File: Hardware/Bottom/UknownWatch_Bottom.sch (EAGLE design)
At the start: 31 parts, among them U1 AD5242-SO16

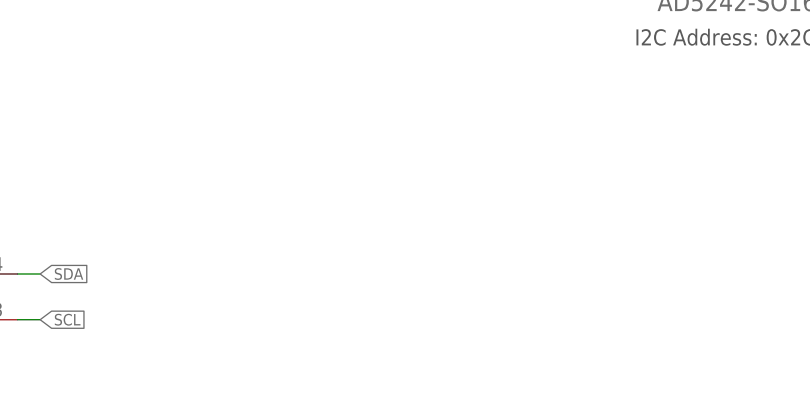
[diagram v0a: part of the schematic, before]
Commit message: Added connections from bottom to top board and other various changes.
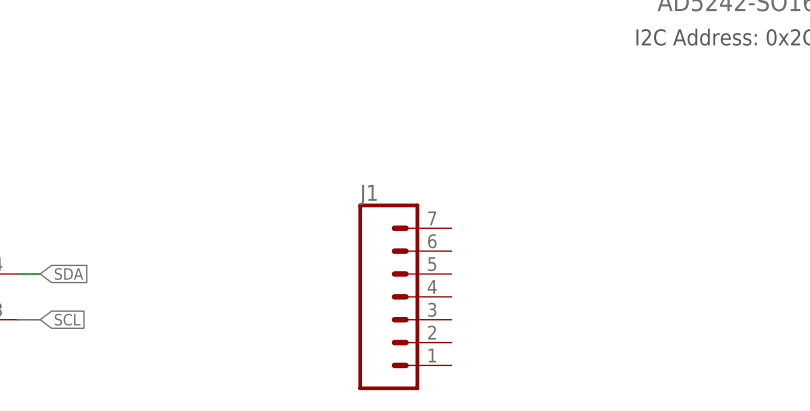
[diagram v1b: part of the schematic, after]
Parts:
- added J1: (no value), LinnesLab-Connectors:CONN_07
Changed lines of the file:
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@@
 <part name="GND2" library="LinnesLab-Symbols" deviceset="GND" device=""/>
 <part name="SUPPLY3" library="LinnesLab-Symbols" deviceset="3.3V" device=""/>
+<part name="J1" library="LinnesLab-Connectors" deviceset="CONN_07" device=""/>
 </parts>
 <sheets>
@@
 <attribute name="VALUE" x="5.08" y="-12.446" size="1.778" layer="96" align="bottom-center"/>
 </instance>
+<instance part="J1" gate="G$1" x="86.36" y="-25.4" smashed="yes">
+<attribute name="VALUE" x="81.28" y="-35.306" size="1.778" layer="96" font="vector"/>
+<attribute name="NAME" x="81.28" y="-12.192" size="1.778" layer="95" font="vector"/>
+</instance>
 </instances>

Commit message: Made all changes associated wih take 002
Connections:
- removed net LED.CTRL: U$4.A
- removed net TIA: C10.2, C15.1, OP4G$1.OUT, U1.W1
- new net A6/TIA: C10.2, C15.1, J1.5, OP4G$1.OUT, U1.W1
- new net A7/PPG: C21.2, J1.7, OP3G$1.OUT
- new net D29/LED.CTRL: J1.6, U$4.A
- net PPG: no longer C21.2, OP3G$1.OUT
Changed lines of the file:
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@@
 </segment>
 </net>
-<net name="TIA" class="0">
+<net name="A6/TIA" class="0">
 <segment>
 <wire x1="109.22" y1="27.94" x2="104.14" y2="27.94" width="0.1524" layer="91"/>
@@
 <junction x="55.88" y="93.98"/>
 </segment>
+<segment>
+<pinref part="J1" gate="G$1" pin="5"/>
+<wire x1="91.44" y1="-20.32" x2="93.98" y2="-20.32" width="0.1524" layer="91"/>
+<label x="93.98" y="-20.32" size="1.27" layer="95" xref="yes"/>
+</segment>
 </net>
 <net name="PD.C" class="0">
@@
 </segment>
 </net>
-<net name="LED.CTRL" class="0">
+<net name="D29/LED.CTRL" class="0">
 <segment>
 <pinref part="U$4" gate="G$1" pin="A"/>
@@
 <wire x1="205.74" y1="30.48" x2="205.74" y2="38.1" width="0.1524" layer="91"/>
 <label x="205.74" y="38.1" size="1.27" layer="95" rot="R180" xref="yes"/>
+</segment>
+<segment>
+<pinref part="J1" gate="G$1" pin="6"/>
+<wire x1="91.44" y1="-17.78" x2="93.98" y2="-17.78" width="0.1524" layer="91"/>
+<label x="93.98" y="-17.78" size="1.27" layer="95" xref="yes"/>
 </segment>
 </net>
@@
 <label x="139.7" y="27.94" size="1.27" layer="95" xref="yes"/>
 <pinref part="U1" gate="G$1" pin="B2"/>
-</segment>
-<segment>
-<pinref part="C21" gate="G$1" pin="2"/>
-<wire x1="187.96" y1="96.52" x2="195.58" y2="96.52" width="0.1524" layer="91"/>
-<wire x1="195.58" y1="96.52" x2="195.58" y2="86.36" width="0.1524" layer="91"/>
-<pinref part="OP3" gate="G$1" pin="OUT"/>
-<wire x1="195.58" y1="86.36" x2="193.04" y2="86.36" width="0.1524" layer="91"/>
-<wire x1="195.58" y1="96.52" x2="195.58" y2="106.68" width="0.1524" layer="91"/>
-<junction x="195.58" y="96.52"/>
-<label x="195.58" y="106.68" size="1.27" layer="95" rot="R180" xref="yes"/>
-<label x="195.58" y="86.36" size="1.27" layer="95" xref="yes"/>
 </segment>
 </net>
@@
 </segment>
 </net>
+<net name="A7/PPG" class="0">
+<segment>
+<pinref part="C21" gate="G$1" pin="2"/>
+<wire x1="187.96" y1="96.52" x2="195.58" y2="96.52" width="0.1524" layer="91"/>
+<wire x1="195.58" y1="96.52" x2="195.58" y2="86.36" width="0.1524" layer="91"/>
+<pinref part="OP3" gate="G$1" pin="OUT"/>
+<wire x1="195.58" y1="86.36" x2="193.04" y2="86.36" width="0.1524" layer="91"/>
+<wire x1="195.58" y1="96.52" x2="195.58" y2="106.68" width="0.1524" layer="91"/>
+<junction x="195.58" y="96.52"/>
+<label x="195.58" y="106.68" size="1.27" layer="95" rot="R180" xref="yes"/>
+<label x="195.58" y="86.36" size="1.27" layer="95" xref="yes"/>
+</segment>
+<segment>
+<pinref part="J1" gate="G$1" pin="7"/>
+<wire x1="91.44" y1="-15.24" x2="93.98" y2="-15.24" width="0.1524" layer="91"/>
+<label x="93.98" y="-15.24" size="1.27" layer="95" xref="yes"/>
+</segment>
+</net>

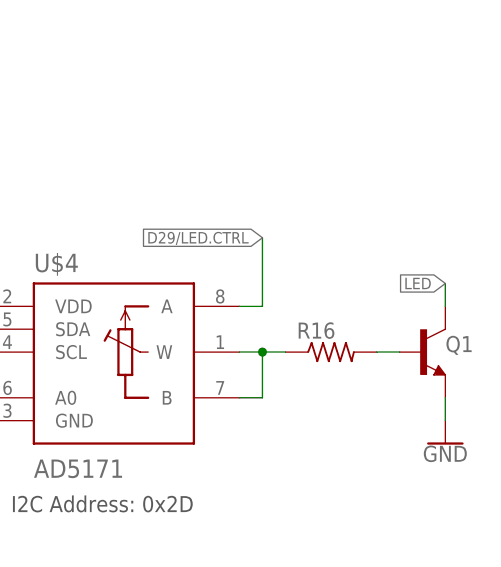
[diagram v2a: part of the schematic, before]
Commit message: Worked on routing for bottom board.
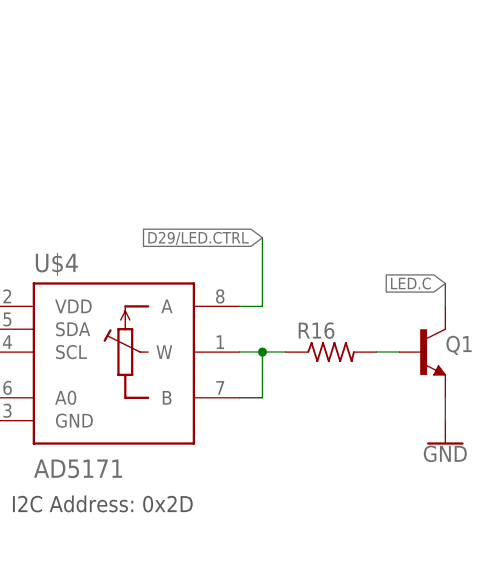
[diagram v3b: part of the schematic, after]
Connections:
- removed net LED: Q1.C
- net LED.C: now also Q1.C
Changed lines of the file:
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@@
 <label x="10.16" y="93.98" size="1.27" layer="95" xref="yes"/>
+</segment>
+<segment>
+<wire x1="226.06" y1="30.48" x2="226.06" y2="33.02" width="0.1524" layer="91"/>
+<label x="226.06" y="33.02" size="1.27" layer="95" rot="R180" xref="yes"/>
+<pinref part="Q1" gate="G$1" pin="C"/>
 </segment>
 </net>
@@
 </segment>
 </net>
-<net name="LED" class="0">
-<segment>
-<wire x1="226.06" y1="30.48" x2="226.06" y2="33.02" width="0.1524" layer="91"/>
-<label x="226.06" y="33.02" size="1.27" layer="95" rot="R180" xref="yes"/>
-<pinref part="Q1" gate="G$1" pin="C"/>
-</segment>
-</net>

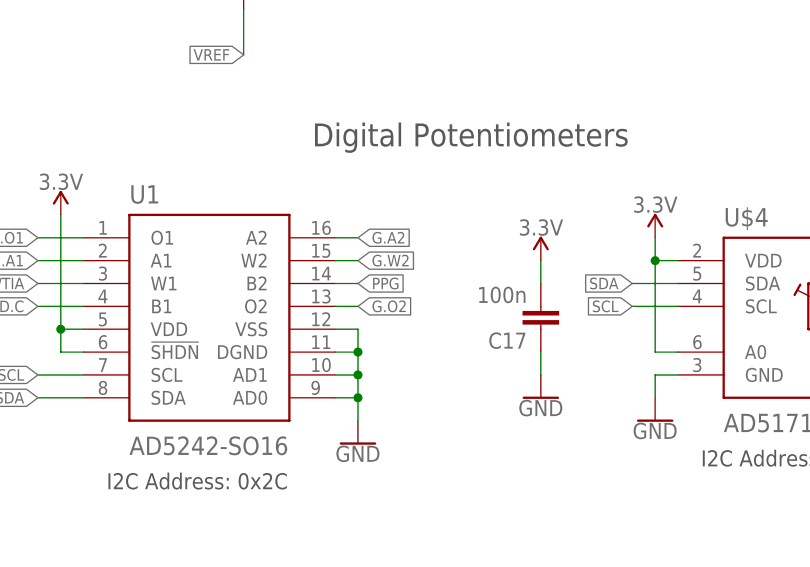
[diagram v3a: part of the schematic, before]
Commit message: Routed more of the bottom board
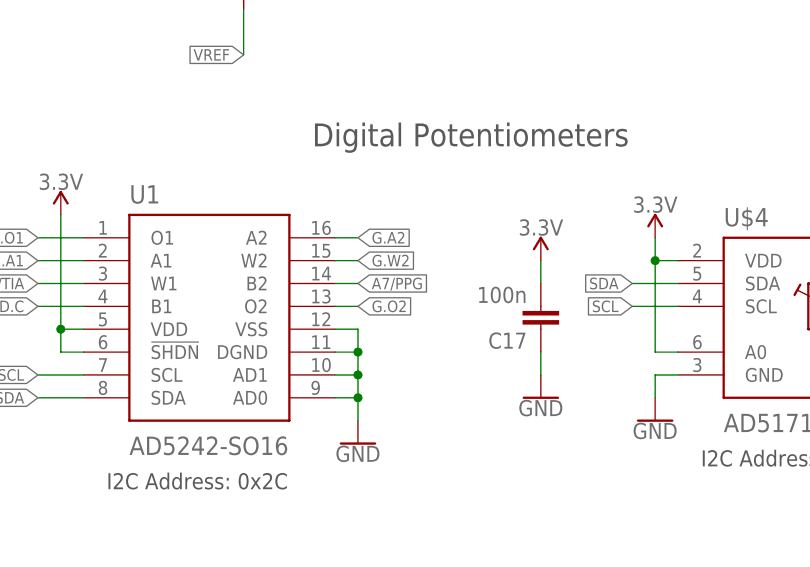
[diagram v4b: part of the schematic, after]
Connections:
- removed net PPG: U1.B2
- net A7/PPG: now also U1.B2
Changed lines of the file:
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@@
-</segment>
-</net>
-<net name="PPG" class="0">
-<segment>
-<wire x1="137.16" y1="27.94" x2="139.7" y2="27.94" width="0.1524" layer="91"/>
-<label x="139.7" y="27.94" size="1.27" layer="95" xref="yes"/>
-<pinref part="U1" gate="G$1" pin="B2"/>
 </segment>
 </net>
@@
 <label x="93.98" y="-15.24" size="1.27" layer="95" xref="yes"/>
 </segment>
+<segment>
+<wire x1="137.16" y1="27.94" x2="139.7" y2="27.94" width="0.1524" layer="91"/>
+<label x="139.7" y="27.94" size="1.27" layer="95" xref="yes"/>
+<pinref part="U1" gate="G$1" pin="B2"/>
+</segment>
 </net>

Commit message: Worked on routing of bottom board
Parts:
- J1: device LinnesLab-Connectors:CONN_07 -> LinnesLab-Connectors:CONN_07-1.27MM
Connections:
- net 3.3V: now also J1.4
- net GND: now also J1.3
- net SCL: now also J1.2
- net SDA: now also J1.1
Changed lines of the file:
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@@
 <part name="GND2" library="LinnesLab-Symbols" deviceset="GND" device=""/>
 <part name="SUPPLY3" library="LinnesLab-Symbols" deviceset="3.3V" device=""/>
-<part name="J1" library="LinnesLab-Connectors" deviceset="CONN_07" device=""/>
+<part name="J1" library="LinnesLab-Connectors" deviceset="CONN_07" device="-1.27MM"/>
+<part name="GND3" library="LinnesLab-Symbols" deviceset="GND" device=""/>
+<part name="SUPPLY1" library="LinnesLab-Symbols" deviceset="3.3V" device=""/>
 </parts>
 <sheets>
@@
 <attribute name="NAME" x="81.28" y="-12.192" size="1.778" layer="95" font="vector"/>
 </instance>
+<instance part="GND3" gate="G$1" x="91.44" y="-38.1" smashed="yes">
+<attribute name="VALUE" x="91.44" y="-38.354" size="1.778" layer="96" align="top-center"/>
+</instance>
+<instance part="SUPPLY1" gate="G$1" x="91.44" y="-10.16" smashed="yes">
+<attribute name="VALUE" x="91.44" y="-7.366" size="1.778" layer="96" align="bottom-center"/>
+</instance>
 </instances>
 <busses>
@@
 <wire x1="5.08" y1="-27.94" x2="5.08" y2="-25.4" width="0.1524" layer="91"/>
 </segment>
+<segment>
+<pinref part="J1" gate="G$1" pin="3"/>
+<pinref part="GND3" gate="G$1" pin="GND"/>
+<wire x1="91.44" y1="-25.4" x2="91.44" y2="-35.56" width="0.1524" layer="91"/>
+</segment>
 </net>
 <net name="3.3V" class="0">
@@
 <wire x1="5.08" y1="-15.24" x2="5.08" y2="-17.78" width="0.1524" layer="91"/>
 </segment>
+<segment>
+<pinref part="J1" gate="G$1" pin="4"/>
+<pinref part="SUPPLY1" gate="G$1" pin="3.3V"/>
+<wire x1="91.44" y1="-22.86" x2="91.44" y2="-10.16" width="0.1524" layer="91"/>
+</segment>
 </net>
 <net name="SDA" class="0">
@@
 <label x="45.72" y="-20.32" size="1.27" layer="95" xref="yes"/>
 </segment>
+<segment>
+<pinref part="J1" gate="G$1" pin="1"/>
+<wire x1="91.44" y1="-30.48" x2="93.98" y2="-30.48" width="0.1524" layer="91"/>
+<label x="93.98" y="-30.48" size="1.27" layer="95" xref="yes"/>
+</segment>
 </net>
 <net name="SCL" class="0">
@@
 <label x="45.72" y="-25.4" size="1.27" layer="95" xref="yes"/>
 </segment>
+<segment>
+<pinref part="J1" gate="G$1" pin="2"/>
+<wire x1="91.44" y1="-27.94" x2="93.98" y2="-27.94" width="0.1524" layer="91"/>
+<label x="93.98" y="-27.94" size="1.27" layer="95" xref="yes"/>
+</segment>
 </net>

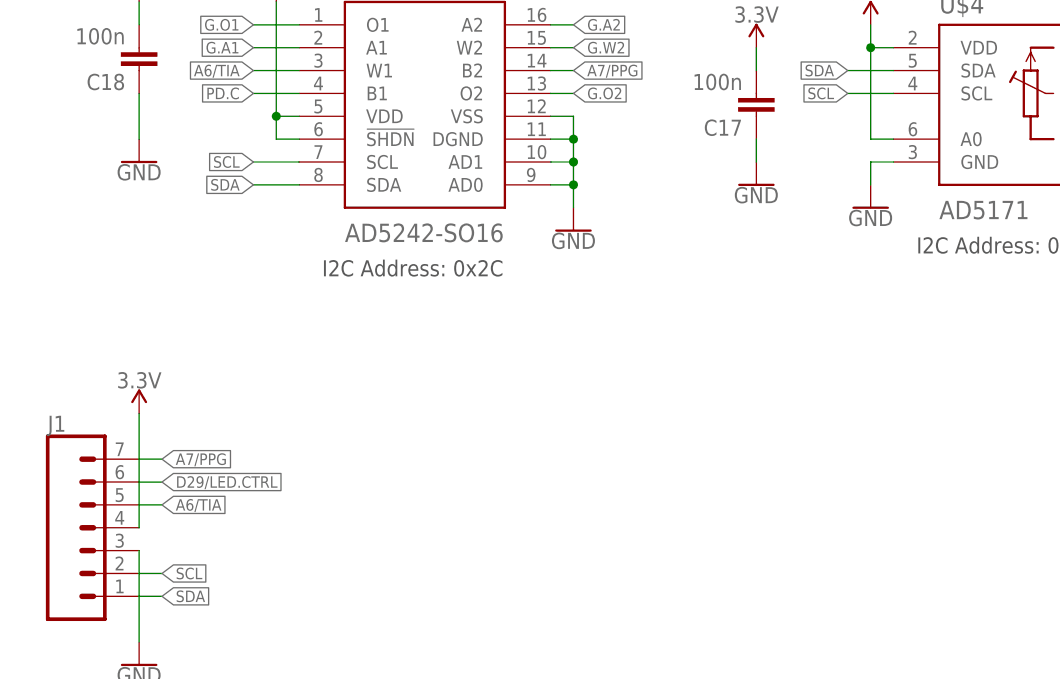
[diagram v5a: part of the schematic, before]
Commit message: Routed more of bottom board
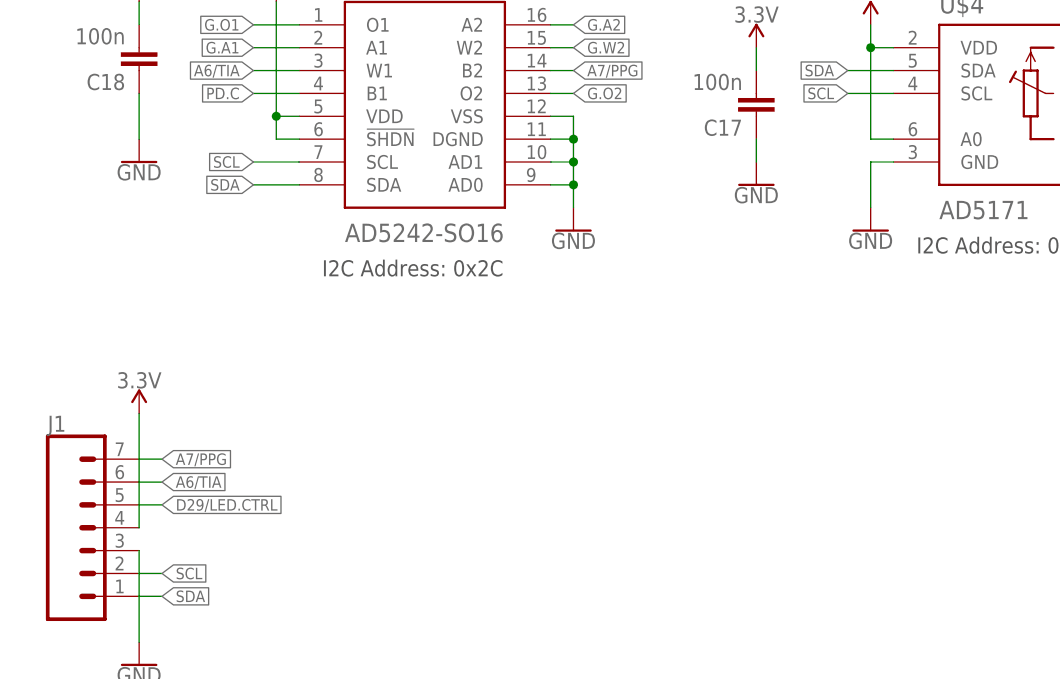
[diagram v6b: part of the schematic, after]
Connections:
- net A6/TIA: now also J1.6; no longer J1.5
- net D29/LED.CTRL: now also J1.5; no longer J1.6
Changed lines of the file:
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@@
 <attribute name="VALUE" x="172.72" y="35.814" size="1.778" layer="96" align="bottom-center"/>
 </instance>
-<instance part="GND19" gate="G$1" x="172.72" y="12.7" smashed="yes">
-<attribute name="VALUE" x="172.72" y="12.446" size="1.778" layer="96" align="top-center"/>
+<instance part="GND19" gate="G$1" x="172.72" y="10.16" smashed="yes">
+<attribute name="VALUE" x="172.72" y="9.906" size="1.778" layer="96" align="top-center"/>
 </instance>
 <instance part="R17" gate="G$1" x="38.1" y="35.56" smashed="yes" rot="R90">
@@
 <wire x1="175.26" y1="17.78" x2="172.72" y2="17.78" width="0.1524" layer="91"/>
 <pinref part="GND19" gate="G$1" pin="GND"/>
-<wire x1="172.72" y1="17.78" x2="172.72" y2="15.24" width="0.1524" layer="91"/>
+<wire x1="172.72" y1="17.78" x2="172.72" y2="12.7" width="0.1524" layer="91"/>
 </segment>
 <segment>
@@
 </segment>
 <segment>
-<pinref part="J1" gate="G$1" pin="5"/>
-<wire x1="91.44" y1="-20.32" x2="93.98" y2="-20.32" width="0.1524" layer="91"/>
-<label x="93.98" y="-20.32" size="1.27" layer="95" xref="yes"/>
+<pinref part="J1" gate="G$1" pin="6"/>
+<wire x1="91.44" y1="-17.78" x2="93.98" y2="-17.78" width="0.1524" layer="91"/>
+<label x="93.98" y="-17.78" size="1.27" layer="95" xref="yes"/>
 </segment>
 </net>
@@
 </segment>
 <segment>
-<pinref part="J1" gate="G$1" pin="6"/>
-<wire x1="91.44" y1="-17.78" x2="93.98" y2="-17.78" width="0.1524" layer="91"/>
-<label x="93.98" y="-17.78" size="1.27" layer="95" xref="yes"/>
-</segment>
-</net>
+<pinref part="J1" gate="G$1" pin="5"/>
+<wire x1="91.44" y1="-20.32" x2="93.98" y2="-20.32" width="0.1524" layer="91"/>
+<label x="93.98" y="-20.32" size="1.27" layer="95" xref="yes"/>
+</segment>
+</net>
